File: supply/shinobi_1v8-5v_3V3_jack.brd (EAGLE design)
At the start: 40.5 x 35 mm, 21 parts, among them P1 POLYSWITCH1210

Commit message: Update.
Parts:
- added R6: 0, FaBo-Resistors:0603-NARROW
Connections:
- net GND: now also R6.1
- net PS: now also R6.2
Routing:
- net PS: track 36.0 -> 17.4 mm, vias 0 -> 2
- net GND: track 114.2 -> 101.7 mm, vias 2 -> 0
- net VIN: track 30.3 -> 31.5 mm
- net VINA: track 9.68 -> 9.99 mm, vias 2 -> 0

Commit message: Update.
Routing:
- net VIN: track 31.5 -> 47.0 mm
- net VOUT: track 53.2 -> 63.3 mm
- net FB: track 10.3 -> 17.5 mm
- net N$3: track 4.90 -> 5.52 mm
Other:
- board text added: "VIN"
- board text added: "VOUT"
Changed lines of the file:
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@@
 <text x="12.692" y="29.286" size="2.54" layer="21">#12</text>
 <text x="5.892" y="25.786" size="0.6096" layer="21">Rev 1.0.0.A</text>
+<text x="36" y="11" size="1.778" layer="21">VIN</text>
+<text x="1" y="22" size="1.778" layer="21">VOUT</text>
 </plain>
 <attributes>
@@
 <contactref element="P4" pad="VCC"/>
 <contactref element="P1" pad="P$1"/>
-<wire x1="26.8224" y1="21.0312" x2="26.8224" y2="21.7932" width="0.1524" layer="1"/>
-<wire x1="29.5656" y1="18.288" x2="26.8224" y2="21.0312" width="0.1524" layer="1"/>
+<wire x1="26.8224" y1="21.5496625" x2="26.8224" y2="21.0312" width="0.1524" layer="1"/>
+<wire x1="26.8224" y1="21.5496625" x2="26.8224" y2="21.7932" width="0.1524" layer="1"/>
 <wire x1="26.8224" y1="21.7932" x2="26.7" y2="21.9" width="0.1524" layer="1"/>
 <wire x1="29.5656" y1="18.288" x2="29.6" y2="18.2" width="0.1524" layer="1"/>
+<wire x1="29.6" y1="18.2" x2="29.6" y2="18.4" width="0.8128" layer="1"/>
+<wire x1="29.6" y1="18.4" x2="27" y2="21" width="0.8128" layer="1"/>
+<wire x1="27" y1="21" x2="27" y2="21.3720625" width="0.8128" layer="1"/>
+<wire x1="27" y1="21.3720625" x2="26.8224" y2="21.5496625" width="0.8128" layer="1"/>
 </signal>
 <signal name="N$15">
 <contactref element="M1" pad="D"/>
 <contactref element="P1" pad="P$2"/>
-<wire x1="21.0312" y1="24.9936" x2="26.67" y2="24.9936" width="0.1524" layer="1"/>
-<wire x1="26.67" y1="24.9936" x2="26.7" y2="24.9" width="0.1524" layer="1"/>
+<wire x1="22.665003125" y1="24.9936" x2="21.0312" y2="24.9936" width="0.1524" layer="1"/>
 <wire x1="21.0312" y1="24.9936" x2="21" y2="24.9" width="0.1524" layer="1"/>
+<wire x1="26.7" y1="24.9" x2="22.758603125" y2="24.9" width="0.8128" layer="1"/>
+<wire x1="22.758603125" y1="24.9" x2="22.665003125" y2="24.9936" width="0.8128" layer="1"/>
 </signal>
 <signal name="FB">
@@
 <wire x1="14.0208" y1="8.8392" x2="20.7264" y2="8.8392" width="0.1524" layer="1"/>
 <wire x1="13.716" y1="8.5344" x2="14.0208" y2="8.8392" width="0.1524" layer="1"/>
-<wire x1="20.7264" y1="8.8392" x2="20.8" y2="8.875" width="0.1524" layer="1"/>
+<wire x1="20.8" y1="8.875" x2="20.7264" y2="8.8392" width="0.1524" layer="1"/>
 <wire x1="13.716" y1="8.5344" x2="13.65" y2="8.5" width="0.1524" layer="1"/>
-<wire x1="13.8684" y1="8.8392" x2="11.8872" y2="10.8204" width="0.1524" layer="1"/>
-<wire x1="14.0208" y1="8.8392" x2="13.8684" y2="8.8392" width="0.1524" layer="1"/>
-<wire x1="11.8872" y1="10.8204" x2="11.85" y2="10.9" width="0.1524" layer="1"/>
+<wire x1="13.8684" y1="8.8392" x2="14.0208" y2="8.8392" width="0.1524" layer="1"/>
+<wire x1="11.85" y1="10.9" x2="13.8684" y2="8.8392" width="0.3048" layer="1"/>
+<wire x1="13.65" y1="8.5" x2="20.8" y2="8.875" width="0.3048" layer="1"/>
 </signal>
 <signal name="N$2">
@@
 <wire x1="25.2984" y1="13.1064" x2="25.25" y2="13.1" width="0.1524" layer="1"/>
 <wire x1="25.2984" y1="15.3924" x2="25.25" y2="15.4" width="0.1524" layer="1"/>
-<wire x1="25.146" y1="16.764" x2="25.146" y2="15.5448" width="0.1524" layer="1"/>
-<wire x1="23.3172" y1="18.5928" x2="25.146" y2="16.764" width="0.1524" layer="1"/>
-<wire x1="25.146" y1="15.5448" x2="25.25" y2="15.4" width="0.1524" layer="1"/>
-<wire x1="23.3172" y1="18.5928" x2="23.286" y2="18.7" width="0.1524" layer="1"/>
-<wire x1="26.0604" y1="5.9436" x2="22.86" y2="5.9436" width="0.1524" layer="1"/>
-<wire x1="28.3464" y1="8.2296" x2="26.0604" y2="5.9436" width="0.1524" layer="1"/>
+<wire x1="26.75581875" y1="7.63901875" x2="28.0584" y2="7.9416" width="0.1524" layer="1"/>
+<wire x1="28.0584" y1="7.9416" x2="28.3464" y2="8.2296" width="0.1524" layer="1"/>
 <wire x1="29.718" y1="8.2296" x2="29.2608" y2="8.2296" width="0.1524" layer="1"/>
 <wire x1="29.2608" y1="8.2296" x2="28.3464" y2="8.2296" width="0.1524" layer="1"/>
-<wire x1="30.48" y1="8.9916" x2="29.718" y2="8.2296" width="0.1524" layer="1"/>
-<wire x1="22.86" y1="5.9436" x2="22.8" y2="5.925" width="0.1524" layer="1"/>
+<wire x1="30.46185625" y1="8.97345625" x2="30.48" y2="8.9916" width="0.1524" layer="1"/>
+<wire x1="30.46185625" y1="8.97345625" x2="29.718" y2="8.2296" width="0.1524" layer="1"/>
+<wire x1="22.822090625" y1="5.931846875" x2="22.8" y2="5.925" width="0.1524" layer="1"/>
 <wire x1="30.48" y1="8.9916" x2="30.55" y2="9.1" width="0.1524" layer="1"/>
 <wire x1="30.6324" y1="9.144" x2="30.6324" y2="11.43" width="0.1524" layer="1"/>
@@
 <wire x1="29.2608" y1="8.2296" x2="29.2608" y2="4.8768" width="0.1524" layer="1"/>
 <wire x1="27.1272" y1="2.286" x2="27.1904" y2="2.2" width="0.1524" layer="1"/>
-<wire x1="29.1084" y1="12.954" x2="25.2984" y2="12.954" width="0.1524" layer="1"/>
-<wire x1="30.48" y1="11.5824" x2="29.1084" y2="12.954" width="0.1524" layer="1"/>
+<wire x1="29.8985125" y1="12.954" x2="25.37756875" y2="12.954" width="0.1524" layer="1"/>
+<wire x1="29.8985125" y1="12.954" x2="30.1084" y2="12.954" width="0.1524" layer="1"/>
+<wire x1="25.37756875" y1="12.954" x2="25.2984" y2="12.954" width="0.1524" layer="1"/>
+<wire x1="30.41041875" y1="11.839228125" x2="30.48" y2="11.5824" width="0.1524" layer="1"/>
 <wire x1="25.2984" y1="12.954" x2="25.25" y2="13.1" width="0.1524" layer="1"/>
 <wire x1="30.48" y1="11.5824" x2="30.55" y2="11.5" width="0.1524" layer="1"/>
+<wire x1="23.286" y1="18.218425" x2="23.286" y2="18.7" width="0.8128" layer="1"/>
+<wire x1="25.25" y1="15.4" x2="25.25" y2="16.254425" width="0.8128" layer="1"/>
+<wire x1="25.25" y1="16.254425" x2="23.286" y2="18.218425" width="0.8128" layer="1"/>
+<wire x1="25.25" y1="15.4" x2="25.25" y2="13.08156875" width="0.8128" layer="1"/>
+<wire x1="25.25" y1="13.08156875" x2="25.37756875" y2="12.954" width="0.8128" layer="1"/>
+<wire x1="25.25" y1="13.1" x2="29.7525125" y2="13.1" width="0.8128" layer="1"/>
+<wire x1="29.7525125" y1="13.1" x2="29.8985125" y2="12.954" width="0.8128" layer="1"/>
+<wire x1="29.7525125" y1="13.1" x2="29.9624" y2="13.1" width="0.8128" layer="1"/>
+<wire x1="29.9624" y1="13.1" x2="30.1084" y2="12.954" width="0.8128" layer="1"/>
+<wire x1="30.1084" y1="12.954" x2="30.1084" y2="12.141246875" width="0.8128" layer="1"/>
+<wire x1="30.1084" y1="12.141246875" x2="30.41041875" y2="11.839228125" width="0.8128" layer="1"/>
+<wire x1="30.55" y1="11.5" x2="30.55" y2="9.0616" width="0.8128" layer="1"/>
+<wire x1="30.55" y1="9.0616" x2="30.46185625" y2="8.97345625" width="0.8128" layer="1"/>
+<wire x1="30.55" y1="9.1" x2="30.55" y2="8.55" width="0.8128" layer="1"/>
+<wire x1="30.55" y1="8.55" x2="30" y2="8" width="0.8128" layer="1"/>
+<wire x1="30" y1="8" x2="28.1168" y2="8" width="0.3048" layer="1"/>
+<wire x1="28.1168" y1="8" x2="28.0584" y2="7.9416" width="0.3048" layer="1"/>
+<wire x1="28.0584" y1="7.9416" x2="27.496128125" y2="7.9416" width="0.3048" layer="1"/>
+<wire x1="27.496128125" y1="7.9416" x2="25.777265625" y2="6.2227375" width="0.3048" layer="1"/>
+<wire x1="24.171984375" y1="5.9436" x2="23.9783125" y2="5.9436" width="0.3048" layer="1"/>
+<wire x1="23.9783125" y1="5.9436" x2="23.9049125" y2="6.017" width="0.3048" layer="1"/>
+<wire x1="23.9049125" y1="6.017" x2="22.90724375" y2="6.017" width="0.3048" layer="1"/>
+<wire x1="22.90724375" y1="6.017" x2="22.822090625" y2="5.931846875" width="0.3048" layer="1"/>
+<wire x1="25.777265625" y1="6.2227375" x2="24.451121875" y2="6.2227375" width="0.3048" layer="1"/>
+<wire x1="24.451121875" y1="6.2227375" x2="24.171984375" y2="5.9436" width="0.3048" layer="1"/>
 </signal>
 <signal name="L1">
@@
 <wire x1="14.1732" y1="15.3924" x2="14.1" y2="15.35" width="0.1524" layer="1"/>
 <wire x1="16.4592" y1="15.3924" x2="16.5" y2="15.35" width="0.1524" layer="1"/>
-<wire x1="17.3736" y1="10.9728" x2="13.5636" y2="10.9728" width="0.1524" layer="1"/>
-<wire x1="19.6596" y1="13.2588" x2="17.3736" y2="10.9728" width="0.1524" layer="1"/>
-<wire x1="19.6596" y1="14.6304" x2="19.6596" y2="13.2588" width="0.1524" layer="1"/>
-<wire x1="19.05" y1="15.24" x2="19.6596" y2="14.6304" width="0.1524" layer="1"/>
 <wire x1="13.5636" y1="10.9728" x2="13.55" y2="10.9" width="0.1524" layer="1"/>
-<wire x1="19.05" y1="15.24" x2="18.9" y2="15.35" width="0.1524" layer="1"/>
 <wire x1="18.8976" y1="15.3924" x2="16.6116" y2="15.3924" width="0.1524" layer="1"/>
 <wire x1="16.6116" y1="15.3924" x2="16.5" y2="15.35" width="0.1524" layer="1"/>
@@
 <wire x1="6.7056" y1="18.8976" x2="6.7216" y2="19" width="0.1524" layer="1"/>
 <wire x1="10.5156" y1="15.3924" x2="14.0208" y2="15.3924" width="0.1524" layer="1"/>
-<wire x1="6.858" y1="19.05" x2="10.5156" y2="15.3924" width="0.1524" layer="1"/>
+<wire x1="10.5156" y1="15.3924" x2="10.381346875" y2="15.526653125" width="0.1524" layer="1"/>
 <wire x1="14.0208" y1="15.3924" x2="14.1" y2="15.35" width="0.1524" layer="1"/>
-<wire x1="6.858" y1="19.05" x2="6.7216" y2="19" width="0.1524" layer="1"/>
+<wire x1="6.7216" y1="19" x2="6.908" y2="19" width="0.3048" layer="1"/>
+<wire x1="6.908" y1="19" x2="10.381346875" y2="15.526653125" width="0.3048" layer="1"/>
+<wire x1="10.381346875" y1="15.526653125" x2="18.763346875" y2="15.526653125" width="0.3048" layer="1"/>
+<wire x1="18.763346875" y1="15.526653125" x2="18.8976" y2="15.3924" width="0.3048" layer="1"/>
+<wire x1="18.9" y1="15.35" x2="18.9" y2="15.30713125" width="0.3048" layer="1"/>
+<wire x1="18.9" y1="15.30713125" x2="20.6596" y2="14.54753125" width="0.3048" layer="1"/>
+<wire x1="20.6596" y1="14.54753125" x2="20.6596" y2="13.316503125" width="0.3048" layer="1"/>
+<wire x1="20.6596" y1="13.316503125" x2="17.62564375" y2="11.148140625" width="0.3048" layer="1"/>
+<wire x1="17.62564375" y1="11.148140625" x2="13.5636" y2="10.9728" width="0.3048" layer="1"/>
 </signal>
 </signals>

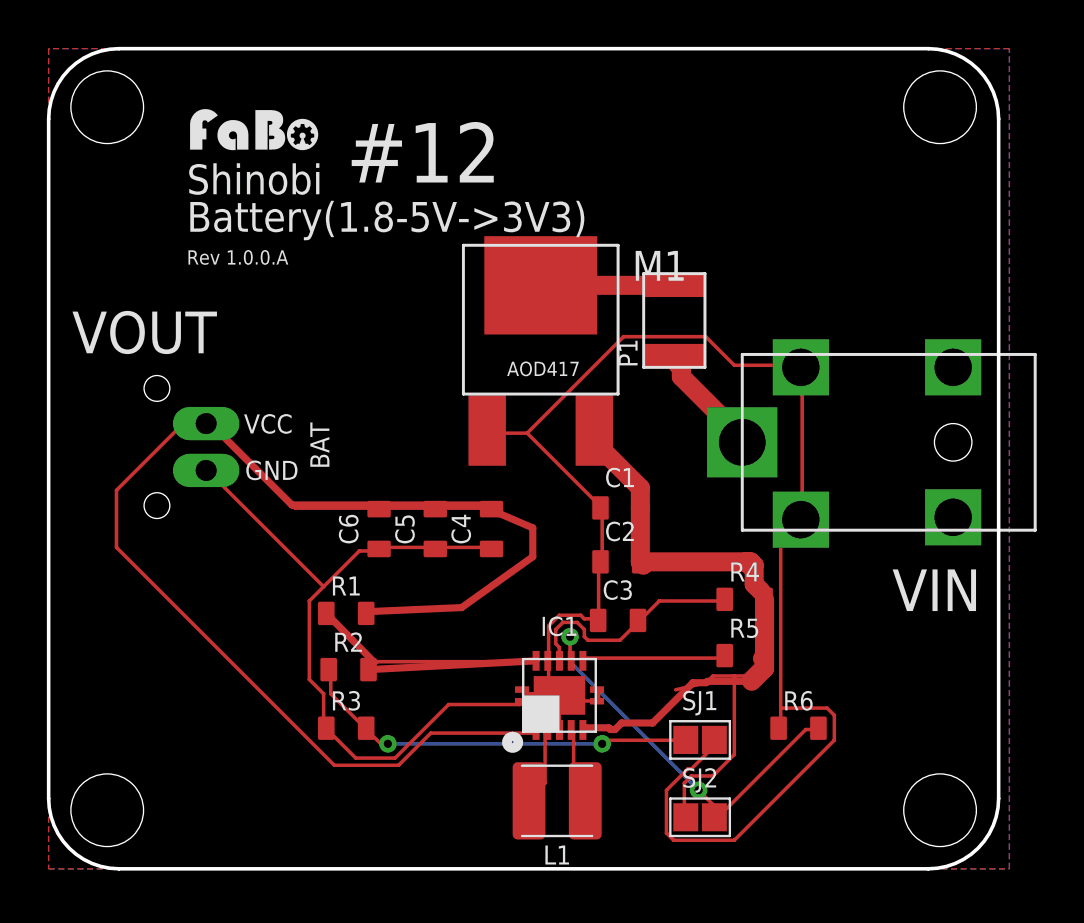
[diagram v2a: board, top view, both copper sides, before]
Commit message: Update 3v3.
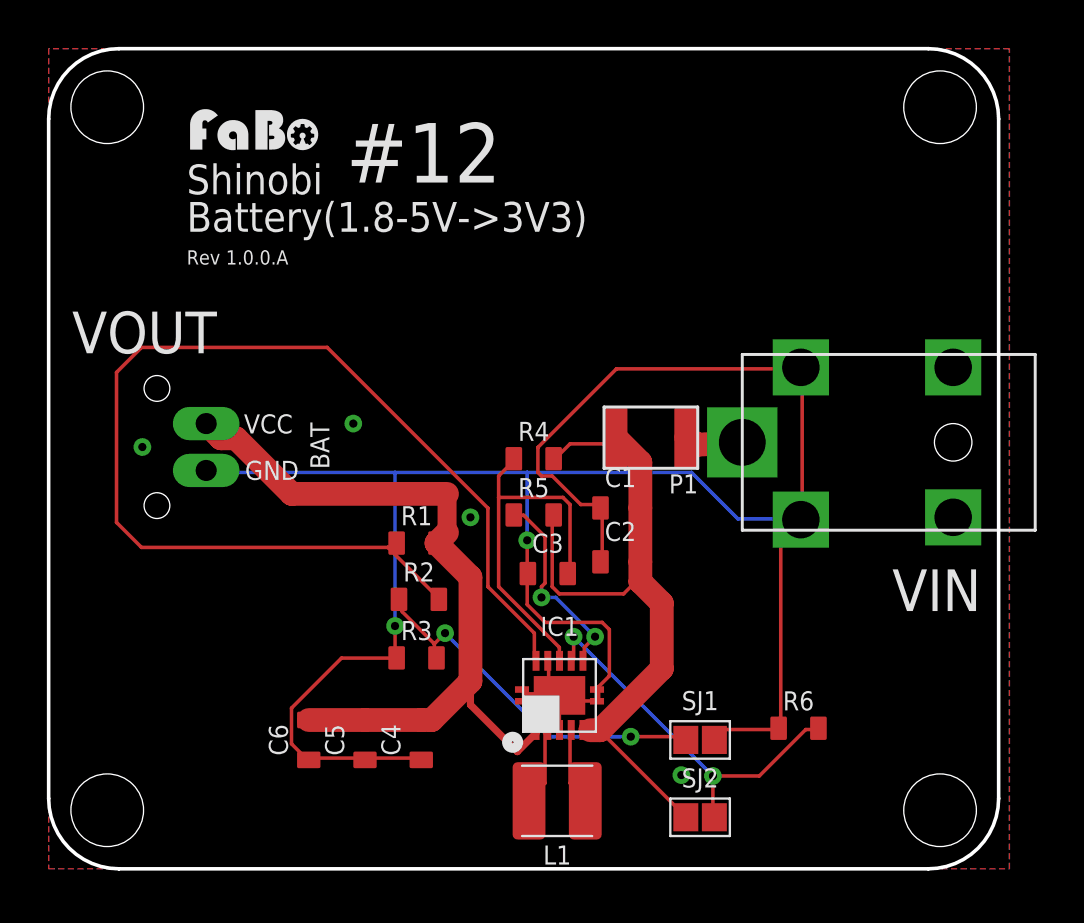
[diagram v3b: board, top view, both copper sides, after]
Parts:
- removed M1: (no value), FaBo-Transistor:AOD417
- moved R4 10.8 mm to (20.7, 17.5)
- moved R5 10.8 mm to (20.7, 15.1)
- moved C5 9.49 mm to (13.5, 5.50)
- moved C6 9.49 mm to (11.1, 5.50)
- moved C4 9.49 mm to (15.9, 5.50)
- moved P1 5.10 mm to (25.7, 18.4), turned to 180 degrees
- moved R1 4.24 mm to (15.7, 13.9)
- moved R2 4.24 mm to (15.8, 11.5)
- moved R3 4.24 mm to (15.7, 9.00)
- moved C3 3.61 mm to (21.3, 12.6)
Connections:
- removed net N$15: M1.D, P1.P$2
- net GND: no longer M1.G
- net VIN: now also P1.P$2; no longer M1.S
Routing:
- net FB: track 17.5 -> 48.5 mm
- net VOUT: track 63.3 -> 33.0 mm
- net VIN: track 47.0 -> 30.5 mm
- net VINA: track 9.99 -> 16.1 mm
- net N$15: track 5.81 -> 0.00 mm
- net GND: track 101.7 -> 105.5 mm, vias 0 -> 6
- net N$3: track 5.52 -> 2.49 mm
- net EN: track 6.19 -> 8.58 mm, vias 0 -> 2
- net N$2: track 17.2 -> 16.0 mm
- net PS: track 17.4 -> 16.6 mm
